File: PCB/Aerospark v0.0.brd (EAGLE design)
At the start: 58.8 x 43.8 mm, 15 parts

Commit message: PCB Version 1.0 - Final
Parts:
- moved JP2 4.69 mm to (53.1, 17.5), turned to 0 degrees
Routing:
- net GND: track 6.13 -> 0.00 mm
- net 3V3: track 41.1 -> 35.7 mm
- net SBD: track 55.2 -> 50.6 mm
- net N$8: track 39.2 -> 34.6 mm
- net N$7: track 20.9 -> 16.9 mm
- net N$2: track 22.1 -> 24.1 mm
- net LOG: track 38.0 -> 39.9 mm, vias 0 -> 2
- net IGNT: track 60.7 -> 58.8 mm
- net N$6: track 5.82 -> 4.10 mm
- net PWR: track 28.6 -> 27.7 mm, vias 1 -> 0
- net 5V: track 52.6 -> 52.2 mm, vias 1 -> 0
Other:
- board size 58.8 x 43.8 mm -> 58.8 x 42.2 mm

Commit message: Updated PCB to v1.1
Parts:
- removed C2: 100 NF, SparkFun-Capacitors:0805
- added C1: 100 NF, SparkFun-Capacitors:0805
- RELAY: value RELAYPTH3 -> (none)
- U$3: value SARANTEL-SR1202 -> JDGA-REMQV-ANTENNA; device Ava:SARANTEL-SR1202 -> Ava:JDGA-RIGID_COMBO_PAD
- moved T1 18.5 mm to (24.9, 37.9)
- moved D4 17.8 mm to (24.8, 30.0)
- moved PWR 6.63 mm to (12.7, 38.7)
- moved LOG 6.63 mm to (12.7, 34.9)
- moved SBD 6.63 mm to (12.7, 31.1)
- moved R1 6.63 mm to (19.1, 38.7)
- moved R4 6.63 mm to (19.1, 27.3)
- moved R2 6.63 mm to (19.1, 34.9)
- moved R3 6.63 mm to (19.1, 31.1)
- moved U$2 6.01 mm to (19.8, 14.0), turned to 90 degrees
- moved JP1 0.18 mm to (4.75, 21.8), turned to 180 degrees
- moved U$3 0.15 mm to (16.5, 3.40), turned to 180 degrees
- renumbered U$1 to RELAY
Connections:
- new net 10_GND: U$2.10_GND
- net 3V3: now also C1.2; no longer C2.2
- net GND: now also C1.1, U$3.P$2, U$3.P$3, U$3.P$4, U$3.P$5; no longer C2.1, U$2.10_GND, U$3.GND1, U$3.GND2
- net LOG: now also JP1.21; no longer JP1.11
- net N$1: now also U$3.P$1; no longer U$3.FEED
- net PWR: now also JP1.23; no longer JP1.7
- net SBD: now also JP1.19; no longer JP1.15
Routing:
- net SBD: track 50.6 -> 6.35 mm, vias 1 -> 0
- net IGNT: track 58.8 -> 18.6 mm
- net LOG: track 39.9 -> 6.86 mm, vias 2 -> 0
- net PWR: track 27.7 -> 7.38 mm
- net PI/RX: track 7.93 -> 25.2 mm
- net 5V: track 52.2 -> 65.0 mm, vias 0 -> 2
- net 3V3: track 35.7 -> 22.9 mm
- net PI/TX: track 11.5 -> 24.2 mm, vias 2 -> 0
- net N$6: track 4.10 -> 16.0 mm
- net N$1: track 15.0 -> 6.45 mm
- net N$8: track 34.6 -> 41.0 mm, vias 0 -> 2

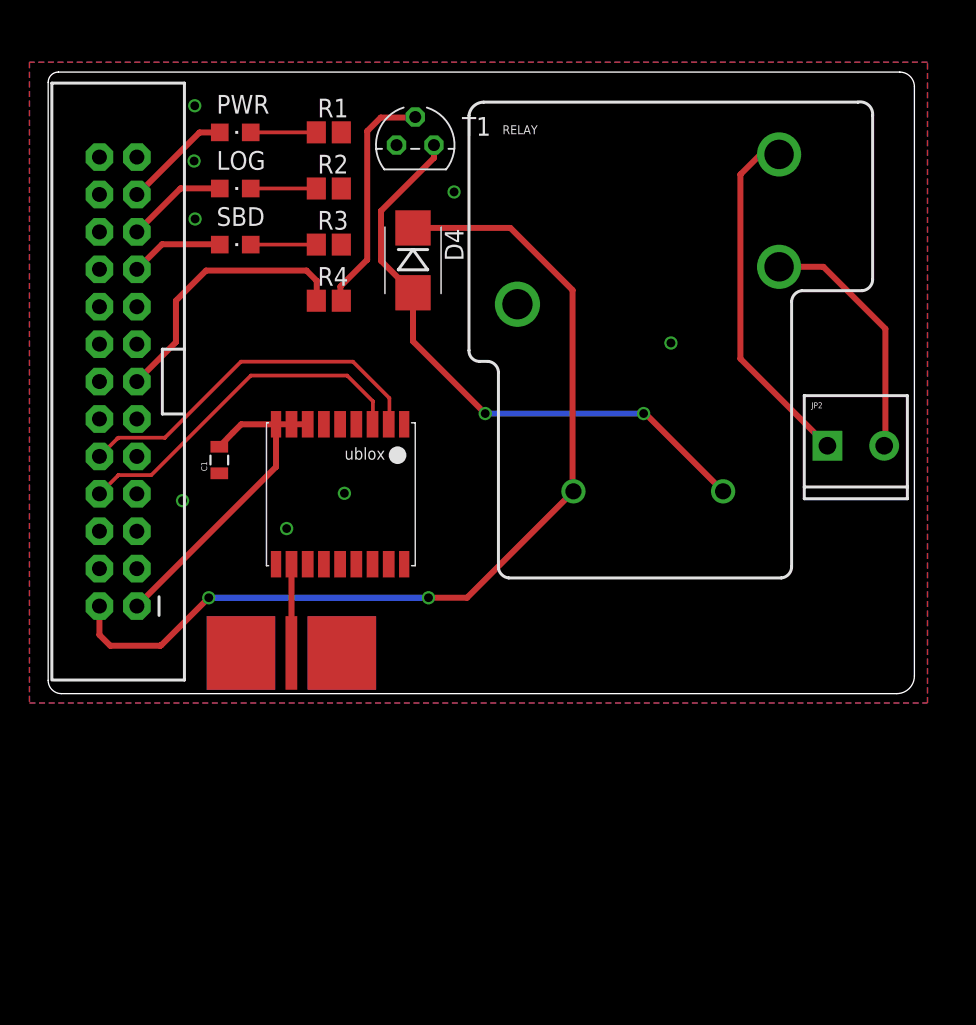
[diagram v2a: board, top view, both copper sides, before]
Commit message: Updated PCB to optoisolator & darlington drivers
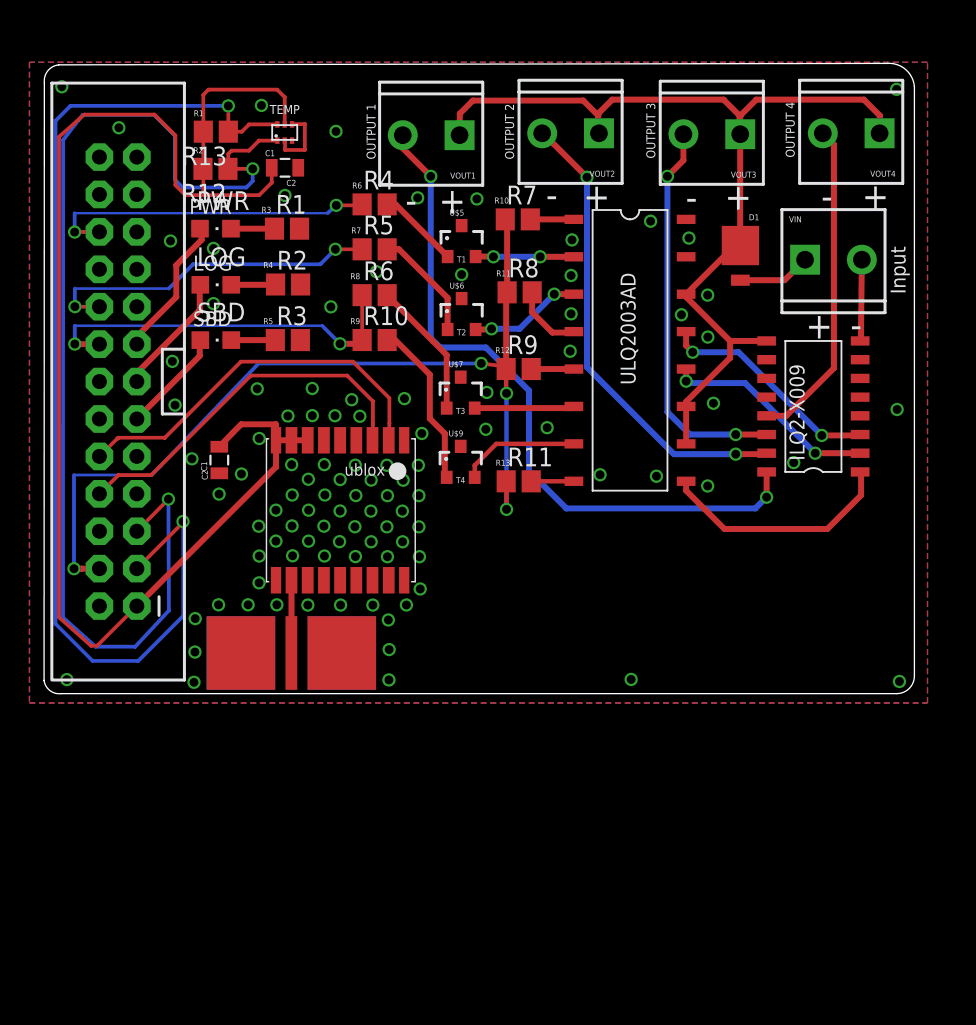
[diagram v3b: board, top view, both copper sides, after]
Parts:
- removed D4: (no value), SparkFun-DiscreteSemi:SMB-DIODE
- removed JP2: Terminal, SparkFun-Connectors:SCREWTERMINAL-3.5MM-2_LOCK
- removed RELAY: (no value), SparkFun-Electromechanical:RELAY-T9A-2
- removed T1: (no value), transistor:TO92
- added C2: (no value), SparkFun-Capacitors:0805
- added R10, R11, R12, R13, R5, R6, R7, R8, R9: (no value), resistor:R0805
- added U$1: ULQ2003A, ULQ2003AD:SOIC
- added U$10: TMP102, TMP102:SOT563
- added U$4: ILQ2-X009, ILQ2-X009:SOIC
- added U$5, U$6, U$7, U$9: (no value), GuShH:SOT-23
- added U$8: (no value), Ava:DO-220AA
- added VIN, VOUT1, VOUT2, VOUT3, VOUT4: (no value), SparkFun-Connectors:SCREWTERMINAL-3.5MM-2_LOCK
- C1: value 100 NF -> (none)
- moved R4 7.24 mm to (22.2, 33.8)
- moved R1 7.13 mm to (16.2, 32.2)
- moved R2 7.08 mm to (16.3, 28.4)
- moved R3 7.05 mm to (16.3, 24.6)
- moved PWR 6.67 mm to (11.4, 32.2)
- moved LOG 6.67 mm to (11.4, 28.4)
- moved SBD 6.62 mm to (11.4, 24.6)
- moved U$2 1.09 mm to (19.8, 12.9)
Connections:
- removed net IGNT: JP1.13, R4.1
- new net N$10: U$4.P$2, U$5.2
- new net N$12: U$4.P$3, U$6.2
- new net N$13: U$4.P$6, U$7.2
- new net N$14: U$1.P$8, VIN.2
- new net N$15: R4.2, U$5.1
- new net N$16: R5.2, U$6.1
- new net N$17: R6.2, U$7.1
- new net N$18: U$8.ANODE, VIN.1
- new net N$20: U$1.P$15, VOUT2.2
- new net N$21: U$1.P$14, VOUT3.2
- new net N$22: U$1.P$13, VOUT4.2
- new net N$24: U$1.P$1, U$4.P$9
- new net N$25: U$1.P$2, U$4.P$12
- new net N$26: U$1.P$3, U$4.P$13
- new net N$27: R10.2, U$9.1
- new net N$28: U$4.P$7, U$9.2
- new net N$29: R11.2, U$4.P$8
- new net OUT1: JP1.22, R4.1
- new net OUT2: JP1.18, R5.1
- new net OUT3: JP1.16, R10.1, R6.1
- new net SCL: JP1.5, R12.1, U$10.P$1
- new net SDA: JP1.3, R13.1, U$10.P$6
- new net VIN: U$1.P$9, U$4.P$10, U$4.P$11, U$4.P$14, U$4.P$15, U$8.CATHODE, VOUT1.1, VOUT2.1, VOUT3.1, VOUT4.1
- net 3V3: now also C2.2, R12.2, R13.2, U$10.P$5
- net 5V: now also R11.1, R7.1, R8.1, R9.1; no longer D4.C, RELAY.COIL1
- net GND: now also C2.1, U$10.P$2, U$10.P$4, U$5.3, U$6.3, U$7.3, U$9.3; no longer T1.3
- net LOG: now also JP1.13; no longer JP1.21
- net N$2: now also R7.2, U$4.P$1; no longer JP2.1, RELAY.NC
- net N$6: now also R8.2, U$4.P$4; no longer R4.2, T1.2
- net N$7: now also R9.2, U$4.P$5; no longer JP2.2, RELAY.NO
- net N$8: now also U$1.P$16, VOUT1.2; no longer D4.A, RELAY.COIL2, T1.1
- net PWR: now also JP1.15; no longer JP1.23
- net SBD: now also JP1.11; no longer JP1.19
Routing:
- net SCL: track 0.00 -> 77.0 mm, vias 0 -> 2
- net 3V3: track 22.9 -> 98.5 mm
- net SDA: track 0.00 -> 73.5 mm, vias 0 -> 2
- net VIN: track 0.00 -> 65.4 mm
- net N$20: track 0.00 -> 31.8 mm, vias 0 -> 2
- net N$21: track 0.00 -> 26.7 mm, vias 0 -> 2
- net OUT3: track 0.00 -> 25.7 mm, vias 0 -> 2
- net OUT2: track 0.00 -> 23.5 mm, vias 0 -> 2
- net OUT1: track 0.00 -> 22.7 mm, vias 0 -> 2
- net N$22: track 0.00 -> 22.2 mm
- net N$2: track 24.1 -> 2.96 mm
- net IGNT: track 18.6 -> 0.00 mm
- net N$24: track 0.00 -> 16.1 mm
- net N$26: track 0.00 -> 15.3 mm, vias 0 -> 2
- net N$25: track 0.00 -> 14.7 mm, vias 0 -> 2
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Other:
- board size 58.8 x 42.2 mm -> 59.1 x 42.8 mm
- board text added: "+"
- board text added: "-"
- board text added: "C1"
- board text added: "C2"
- board text added: "D1"
- board text added: "ILQ2-X009"
- board text added: "Input"
- board text added: "LOG"
- board text added: "OUTPUT 1"
- board text added: "OUTPUT 2"
- board text added: "OUTPUT 3"
- board text added: "OUTPUT 4"
- board text added: "PWR"
- board text added: "R1"
- board text added: "R10"
- board text added: "R11"
- board text added: "R12"
- board text added: "R13"
- board text added: "R2"
- board text added: "R3"
- board text added: "R4"
- board text added: "R5"
- board text added: "R6"
- board text added: "R7"
- board text added: "R8"
- board text added: "R9"
- board text added: "SBD"
- board text added: "T1"
- board text added: "T2"
- board text added: "T3"
- board text added: "T4"
- board text added: "TEMP"
- board text added: "ULQ2003AD"

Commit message: Updated PCB and added mounting hole
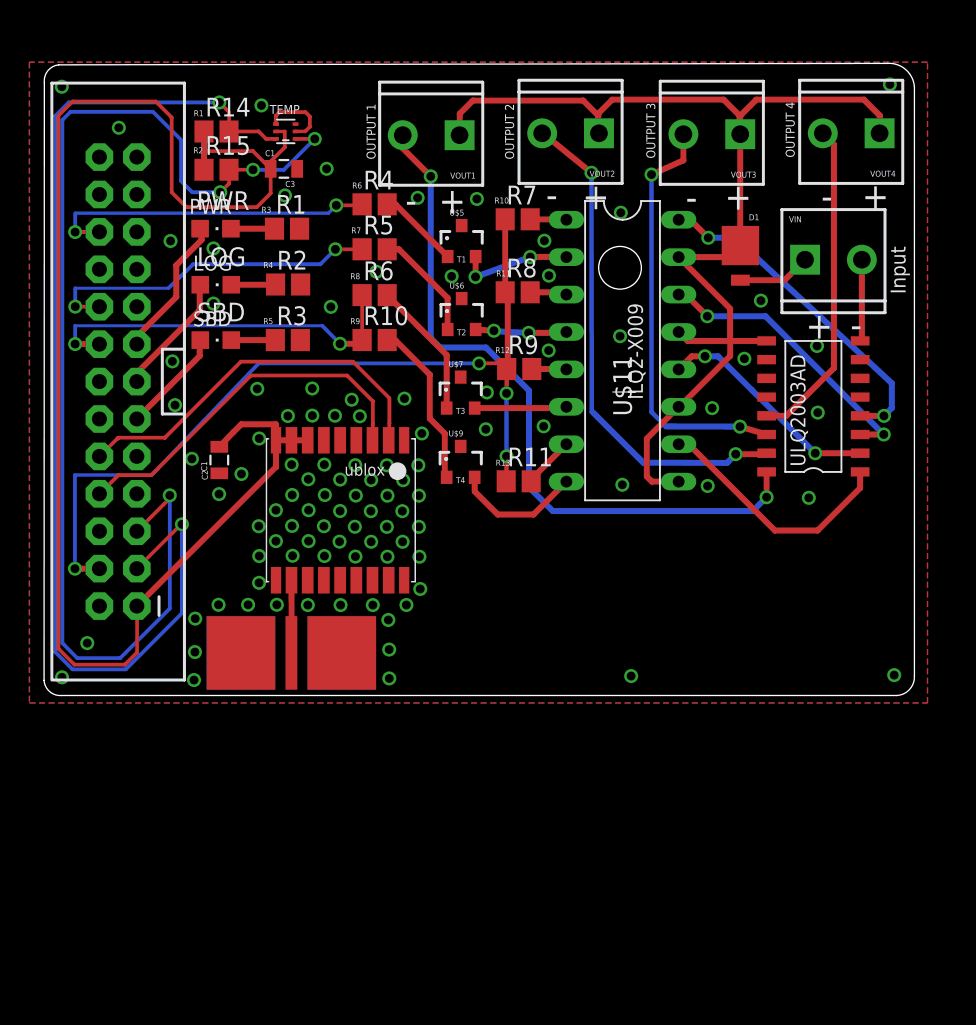
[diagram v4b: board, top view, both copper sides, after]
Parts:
- removed C2: (no value), SparkFun-Capacitors:0805
- removed R12, R13: (no value), resistor:R0805
- removed U$10: TMP102, TMP102:SOT563
- removed U$4: ILQ2-X009, ILQ2-X009:SOIC
- added C3: (no value), SparkFun-Capacitors:0805
- added R14, R15: (no value), resistor:R0805
- added U$11: K847PH, K847PH:DIP16
- added U1: TMP102, SparkFun-Sensors:SOT563
- moved R8 0.13 mm to (31.9, 27.9)
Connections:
- removed net 10_GND: U$2.10_GND
- removed net N$24: U$1.P$1, U$4.P$9
- removed net N$26: U$1.P$3, U$4.P$13
- new net N$11: U$1.P$1, U$11.P$10
- new net N$23: U$1.P$3, U$11.P$14
- new net N$30: U$1.P$4, U$11.P$16
- net 3V3: now also C3.2, R14.1, R15.1, U1.5; no longer C2.2, R12.2, R13.2, U$10.P$5
- net GND: now also C3.1, U$2.10_GND, U1.2, U1.4; no longer C2.1, U$10.P$2, U$10.P$4
- net N$10: now also U$11.P$2; no longer U$4.P$2
- net N$12: now also U$11.P$4; no longer U$4.P$3
- net N$13: now also U$11.P$6; no longer U$4.P$6
- net N$2: now also U$11.P$1; no longer U$4.P$1
- net N$25: now also U$11.P$12; no longer U$4.P$12
- net N$28: now also U$11.P$8; no longer U$4.P$7
- net N$29: now also U$11.P$7; no longer U$4.P$8
- net N$6: now also U$11.P$3; no longer U$4.P$4
- net N$7: now also U$11.P$5; no longer U$4.P$5
- net SCL: now also R15.2, U1.1; no longer R12.1, U$10.P$1
- net SDA: now also R14.2, U1.6; no longer R13.1, U$10.P$6
- net VIN: now also U$11.P$11, U$11.P$13, U$11.P$15, U$11.P$9; no longer U$4.P$10, U$4.P$11, U$4.P$14, U$4.P$15
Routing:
- net N$30: track 0.00 -> 22.9 mm, vias 0 -> 2
- net N$23: track 0.00 -> 19.5 mm, vias 0 -> 2
- net N$11: track 0.00 -> 17.0 mm
- net N$24: track 16.1 -> 0.00 mm
- net N$26: track 15.3 -> 0.00 mm, vias 2 -> 0
- net VIN: track 65.4 -> 77.3 mm
- net 3V3: track 98.5 -> 103.6 mm
- net 5V: track 62.4 -> 59.1 mm
- net SCL: track 77.0 -> 80.3 mm, vias 2 -> 4
- net N$20: track 31.8 -> 34.1 mm
- net N$6: track 4.79 -> 2.61 mm
- net N$21: track 26.7 -> 28.6 mm
- net N$12: track 7.66 -> 6.27 mm
- net N$10: track 6.68 -> 7.83 mm
- net SDA: track 73.5 -> 74.5 mm
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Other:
- board size 59.1 x 42.8 mm -> 59.1 x 42.9 mm
